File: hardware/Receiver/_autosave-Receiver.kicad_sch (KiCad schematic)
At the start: 121 parts, among them J1 USB_C_Receptacle_USB2.0, J3 20021511-00006T4LF, J4 Conn_01x04, J6 JST_PH, Q1 2N7002, Q10 NChan, Q11 NChan, Q2 NChan, Q3 NChan, Q4 NChan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

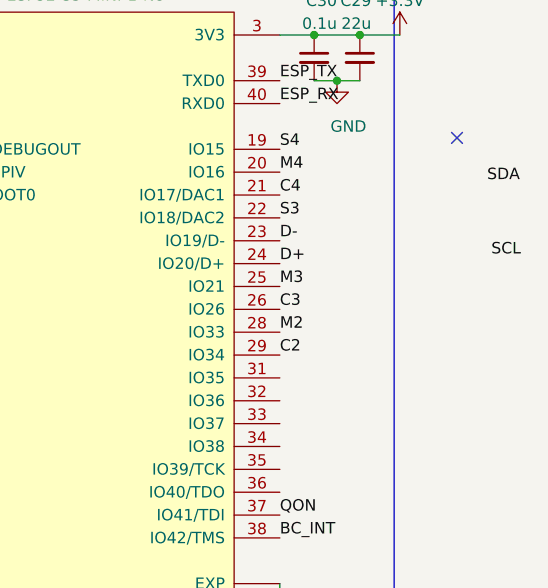
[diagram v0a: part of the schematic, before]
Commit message: update mcu to ESP32S3
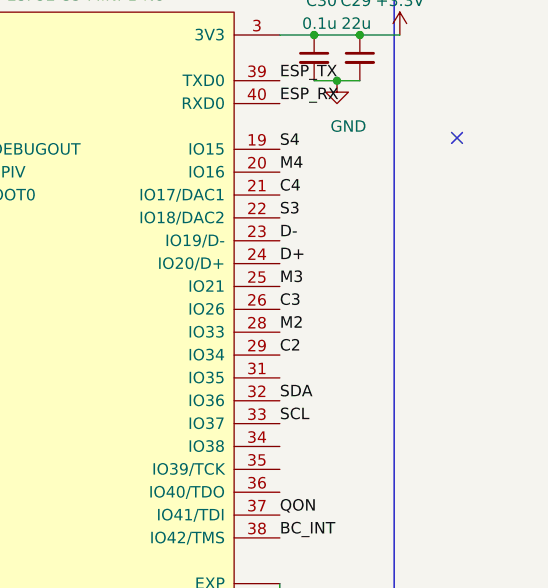
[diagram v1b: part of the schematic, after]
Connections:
- net SCL: now also U7.33 (IO37)
- net SDA: now also U7.32 (IO36)
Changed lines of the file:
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@@
     (effects (font (size 1.27 1.27)) (justify right bottom))
   )
-  (label "SCL" (at 292.1 48.26 0) (fields_autoplaced)
+  (label "SCL" (at 268.605 66.675 0) (fields_autoplaced)
     (effects (font (size 1.27 1.27)) (justify left bottom))
   )
@@
     (effects (font (size 1.27 1.27)) (justify left bottom))
   )
-  (label "SDA" (at 295.275 40.005 180) (fields_autoplaced)
-    (effects (font (size 1.27 1.27)) (justify right bottom))
+  (label "SDA" (at 268.605 64.135 0) (fields_autoplaced)
+    (effects (font (size 1.27 1.27)) (justify left bottom))
   )
   (label "REGN" (at 93.345 130.175 180) (fields_autoplaced)
